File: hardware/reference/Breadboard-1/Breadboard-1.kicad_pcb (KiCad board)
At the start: 2 copper layers, 50.8 x 69.9 mm, 58 parts, among them J1 Left, J2 Right, J3 ICSP, J4 TTL Serial, Q31 HSM0903, Q32 HSM0903, Q41 2N7002, Q42 2N7002, Q43 2N7002, U11 AMS1117-5.0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

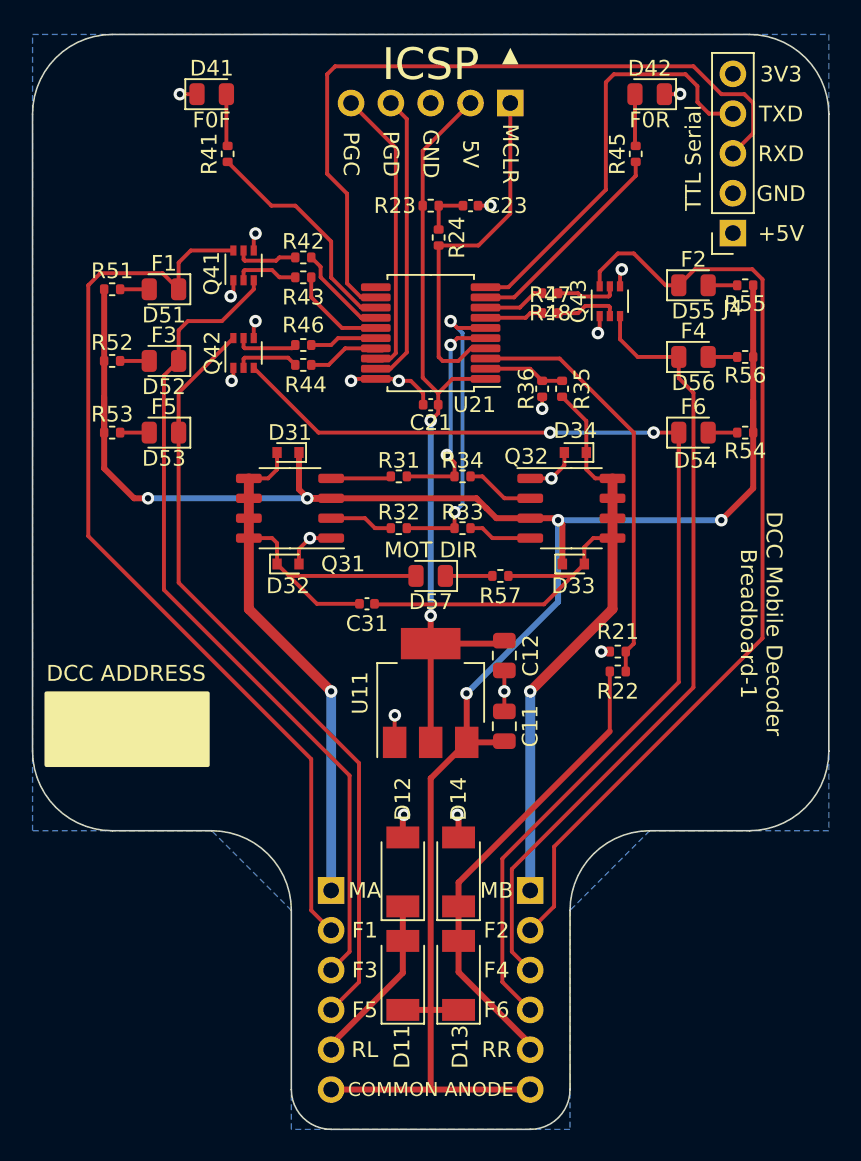
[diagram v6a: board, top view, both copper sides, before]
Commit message: Position cleanup, better trace routing.
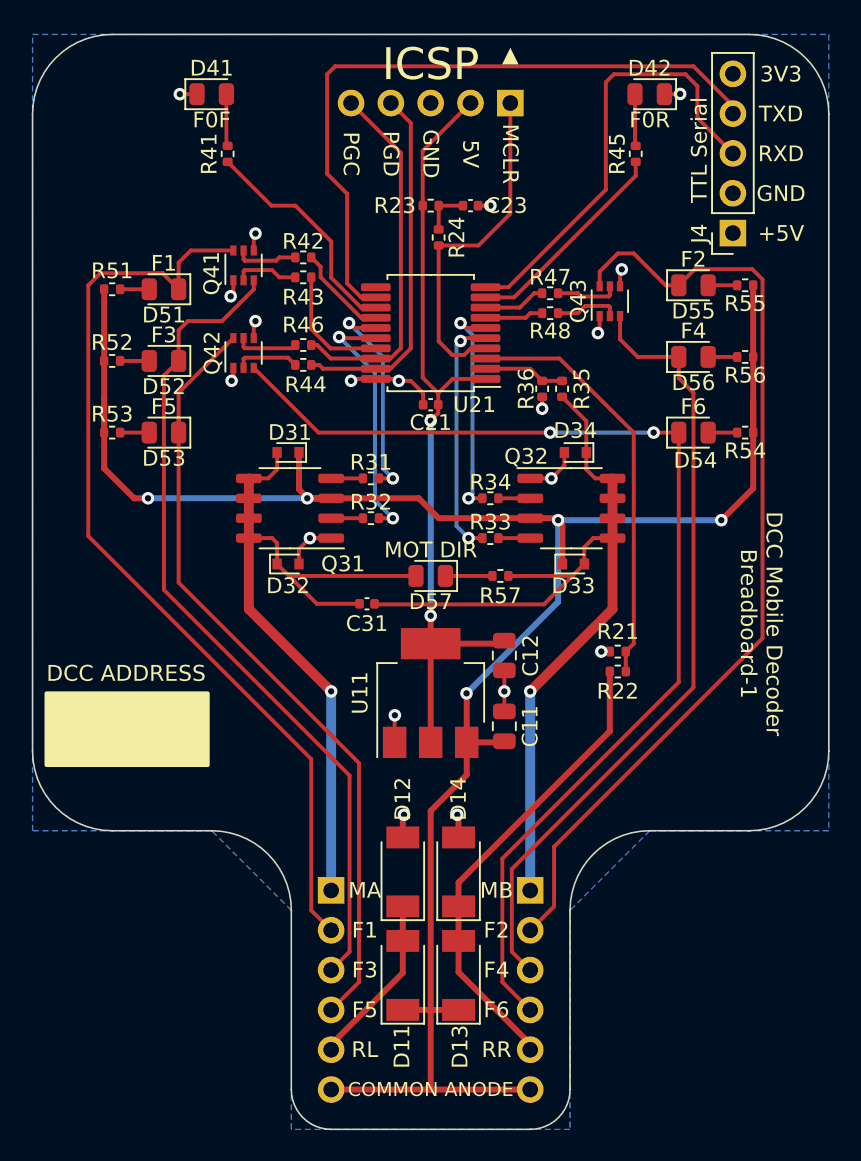
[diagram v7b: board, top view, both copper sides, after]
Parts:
- moved R34 2.26 mm to (80.0, 80.4)
- moved R33 1.89 mm to (80.0, 82.9)
- moved R32 1.89 mm to (72.4, 81.7)
- moved R31 1.78 mm to (72.4, 79.1)
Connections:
- J3 pad 4: PGD -> PGD/F5
- J3 pad 5: PGC -> PGC/F6
- J4 pad 3: RXD -> TXD
- J4 pad 4: TXD -> RXD
- R33 pad 2: P1B -> P1C
- R34 pad 2: P1A -> P1D
- R44 pad 1: F5 -> PGD/F5
- R46 pad 1: F6 -> PGC/F6
- U21 pad 15: F1 -> P1A
- U21 pad 16: F6 -> P1B
- U21 pad 17: F5 -> F1
- U21 pad 18: PGC -> PGC/F6
- U21 pad 19: PGD -> PGD/F5
- U21 pad 5: P1A -> P1C
- U21 pad 6: P1B -> P1D
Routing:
- net PGC/F6: track 0.00 -> 23.3 mm
- net PGD/F5: track 0.00 -> 23.2 mm
- net PGC: track 19.5 -> 0.00 mm
- net PGD: track 18.7 -> 0.00 mm
- net P1C: track 0.00 -> 15.6 mm, vias 0 -> 2
- net P1D: track 0.00 -> 14.2 mm, vias 0 -> 2
- net F5: track 5.49 -> 0.00 mm
- net RXD: track 48.2 -> 43.7 mm
- net F6: track 4.30 -> 0.00 mm
- net P1B: track 19.4 -> 16.2 mm
- net Net-(Q32-Pad2): track 4.39 -> 2.03 mm
- net Net-(Q32-Pad4): track 4.07 -> 2.03 mm
- net Net-(Q31-Pad2): track 4.07 -> 2.03 mm
- net F6_SP: track 73.1 -> 71.1 mm
- net MCLR: track 24.1 -> 22.1 mm
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
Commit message: Added a 100 Ohm load to enable readback when no motor is connected.
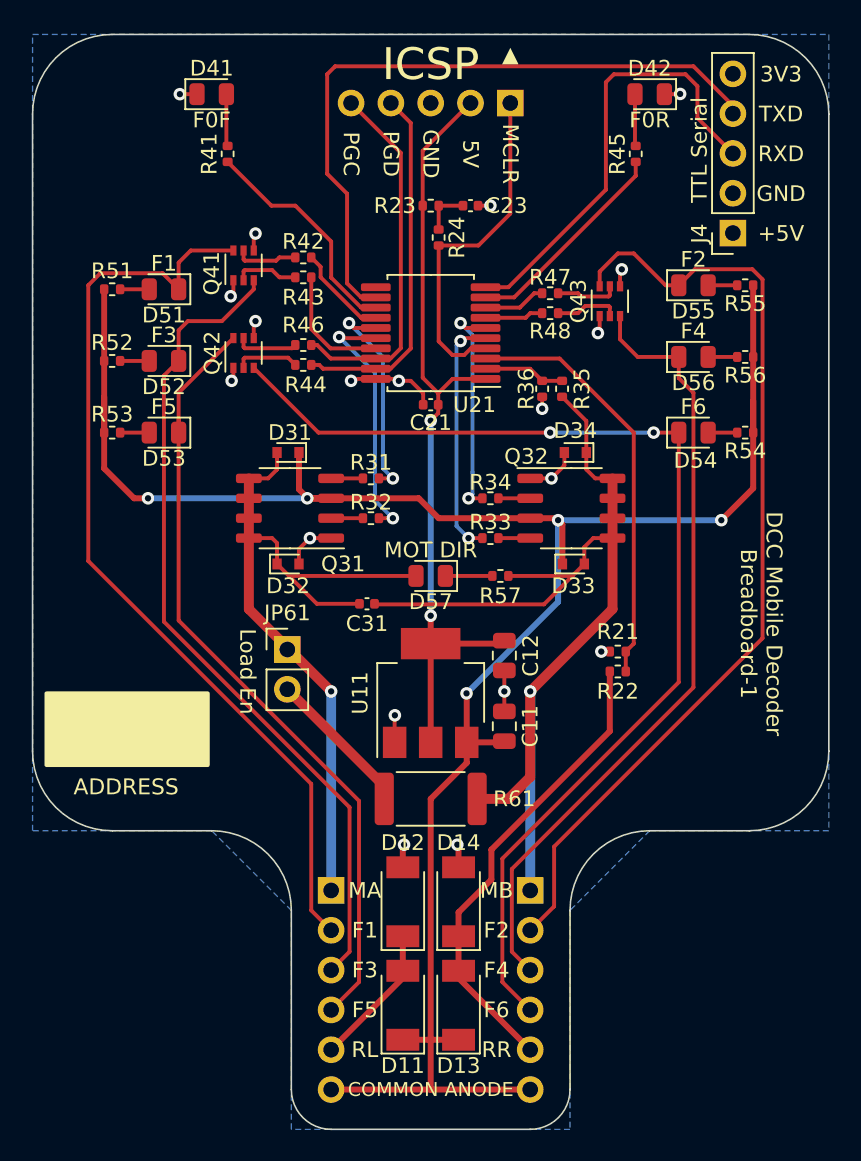
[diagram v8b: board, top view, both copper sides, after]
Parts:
- added JP61: Load En, Connector_PinHeader_2.54mm:PinHeader_1x02_P2.54mm_Vertical, F.Cu at (67.1, 90.0)
- added R61: 100, Resistor_SMD:R_2512_6332Metric, F.Cu at (76.2, 99.6)
- moved D11 1.91 mm to (74.4, 112.7)
- moved D12 1.91 mm to (74.4, 106.1)
- moved D13 1.91 mm to (78.0, 112.7)
- moved D14 1.91 mm to (78.0, 106.1)
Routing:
- net Net-(JP61-Pad2): track 0.00 -> 9.55 mm
- net MOT_B: track 57.1 -> 66.5 mm
- net RAIL_L: track 11.0 -> 9.46 mm
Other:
- board text added: "ADDRESS"
- board text removed: "DCC ADDRESS"
